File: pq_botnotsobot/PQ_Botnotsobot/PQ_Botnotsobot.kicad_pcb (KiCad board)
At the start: 2 copper layers, 64 x 58 mm, 0 parts

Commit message: Functional revision and finishing touches part I
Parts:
- added Annotation1: Silkscreen_Annotation, symbols-nsl:NSL_long, B.Cu at (101.7, 89.6)
- added Annotation2: Silkscreen_Annotation, symbols-nsl:NSL_long, B.Cu at (101.8, 35.2)
- added Annotation3: Silkscreen_Annotation, symbols-nsl:NSL_long, F.Cu at (101.8, 35.1)
- added Annotation4: Silkscreen_Annotation, symbols-nsl:NSL_long, F.Cu at (103.2, 89.5)
- added Annotation5: Silkscreen_Annotation, symbols-nsl:GRSS, F.Cu at (131.5, 54.1)
- added Annotation6: Silkscreen_Annotation, symbols-nsl:IEEE_logo, F.Cu at (131.4, 66.7)
- added Annotation7: Silkscreen_Annotation, symbols-nsl:Bridgemaker, F.Cu at (122.1, 62.1)
- added H1: MountingHole_Pad, MountingHole:MountingHole_2.2mm_M2_Pad, F.Cu at (95.5, 83.3)
- added H2: MountingHole_Pad, MountingHole:MountingHole_2.2mm_M2_Pad, F.Cu at (109.5, 83.3)
- added H3: MountingHole_Pad, MountingHole:MountingHole_2.2mm_M2_Pad, F.Cu at (123.5, 72.3)
- added H4: MountingHole_Pad, MountingHole:MountingHole_2.2mm_M2_Pad, F.Cu at (123.5, 52.3)
- added H5: MountingHole_Pad, MountingHole:MountingHole_2.2mm_M2_Pad, F.Cu at (109.5, 41.3)
- added H6: MountingHole_Pad, MountingHole:MountingHole_2.2mm_M2_Pad, F.Cu at (95.5, 41.3)
- added J1: D2FLA, miscelaneous-nsl:D2FLA, F.Cu at (132.6, 78.3)
- added J2: D2FLA1, miscelaneous-nsl:D2FLA1, F.Cu at (132.6, 46.3)
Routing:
- net (no net): vias 190 -> 0
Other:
- board text added: "DEPLOYER SLIDER PLATE"
- board text removed: "SLIDING BACKPLATE"

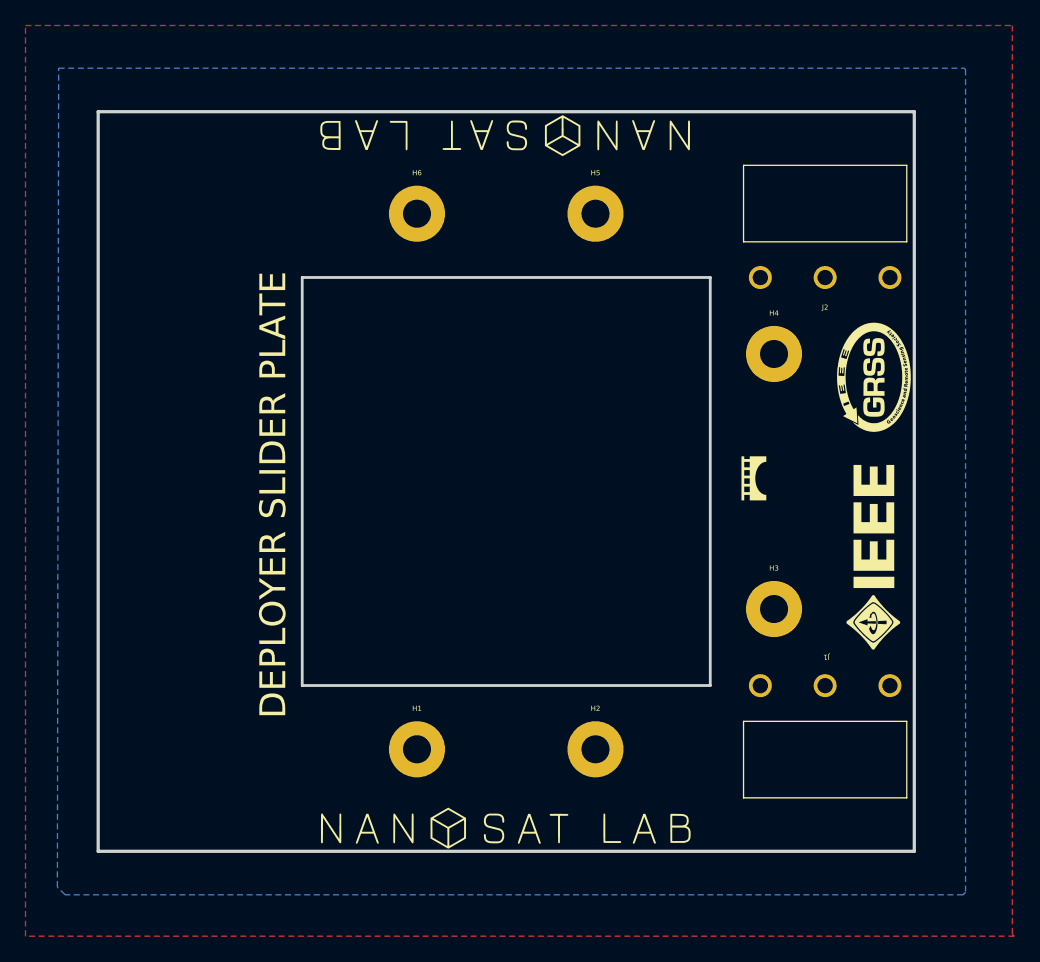
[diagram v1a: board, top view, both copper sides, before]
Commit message: Full Kicad7 transition, library improvement and adaptation, correct footprints and 3D models added
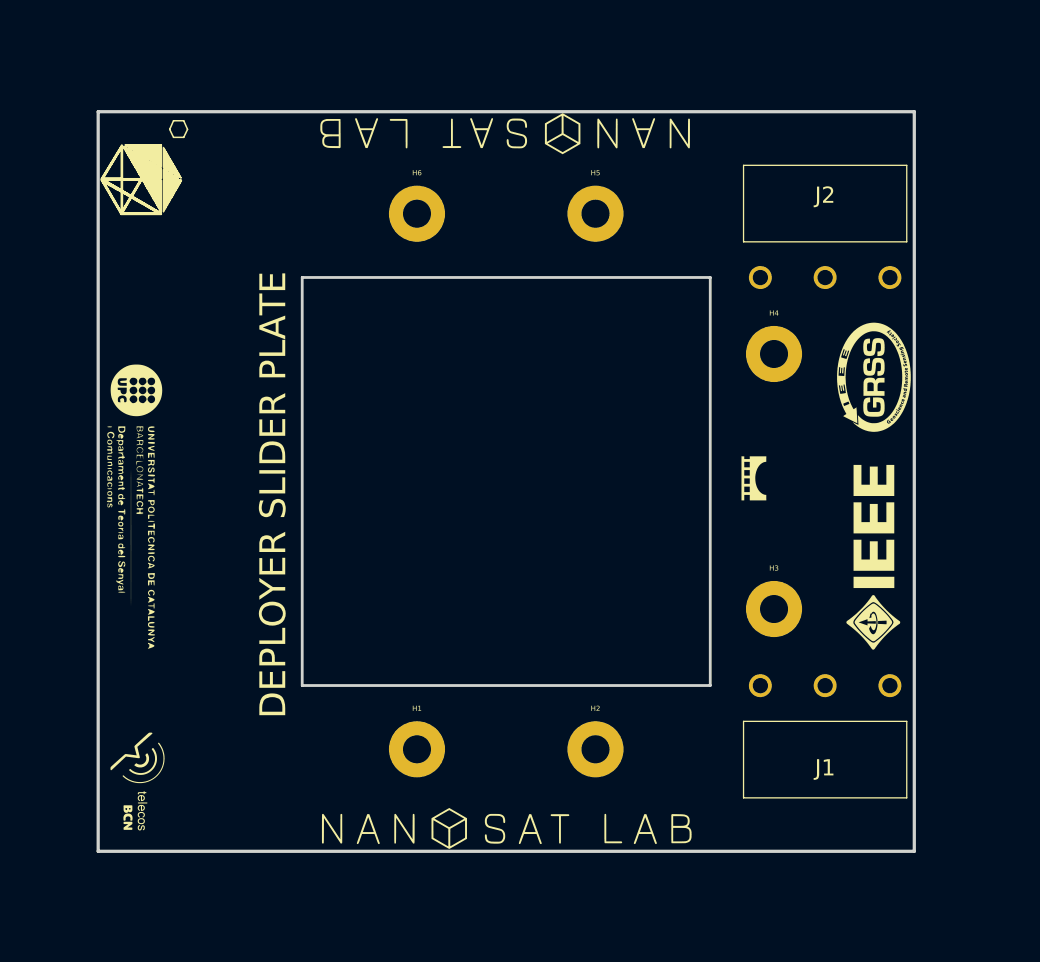
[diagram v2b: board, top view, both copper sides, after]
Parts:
- added Annotation10: Silkscreen_Annotation, -nsl_symbols:NSL, F.Cu at (80.1, 42.7)
- added Annotation8: Silkscreen_Annotation, -nsl_symbols:UPC_positiu, F.Cu at (73.1, 64.0)
- added Annotation9: Silkscreen_Annotation, -nsl_symbols:Telecos, F.Cu at (73.6, 86.1)
- Annotation1, Annotation2, Annotation3, Annotation4: footprint symbols-nsl:NSL_long -> -nsl_symbols:NSL_long
- Annotation5: footprint symbols-nsl:GRSS -> -nsl_symbols:GRSS
- Annotation6: footprint symbols-nsl:IEEE_logo -> -nsl_symbols:IEEE_logo
- Annotation7: footprint symbols-nsl:Bridgemaker -> -nsl_symbols:Bridgemaker
- J1: footprint miscelaneous-nsl:D2FLA -> -nsl_miscellaneous:D2FLA
- J2: footprint miscelaneous-nsl:D2FLA1 -> -nsl_miscellaneous:D2FLA1
- moved Annotation1 0.23 mm to (101.9, 89.6)
- moved Annotation3 0.15 mm to (101.8, 34.9)
- moved Annotation2 0.10 mm to (101.8, 35.1)
- moved Annotation4 0.08 mm to (103.2, 89.6)
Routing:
- removed copper zone on B.Cu, net (none)
- removed copper zone on F.Cu, net (none)

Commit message: fabrication ready
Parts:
- removed Annotation10: Silkscreen_Annotation, -nsl_symbols:NSL
- Annotation5: footprint -nsl_symbols:GRSS -> symbols-nsl:GRSS
- moved Annotation8 8.51 mm to (73.1, 55.4)
- moved Annotation9 8.51 mm to (73.5, 77.6)

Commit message: step and files created for all subsystems
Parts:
- removed Annotation7: Silkscreen_Annotation, -nsl_symbols:Bridgemaker
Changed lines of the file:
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@@
     (grid_origin 70.4596 91.3892)
     (pcbplotparams
-      (layerselection 0x00010fc_ffffffff)
+      (layerselection 0x0001030_7ffffffe)
       (plot_on_all_layers_selection 0x0000000_00000000)
       (disableapertmacros false)
@@
       (hpglpendiameter 15.000000)
       (dxfpolygonmode true)
-      (dxfimperialunits true)
+      (dxfimperialunits false)
       (dxfusepcbnewfont true)
       (psnegative false)
@@
       (sketchpadsonfab false)
       (subtractmaskfromsilk false)
-      (outputformat 1)
+      (outputformat 3)
       (mirror false)
-      (drillshape 1)
+      (drillshape 0)
       (scaleselection 1)
-      (outputdirectory "")
+      (outputdirectory "../../assembly/slider/")
     )
   )
@@
       )
     )
-  )
-  (footprint "-nsl_symbols:Bridgemaker" (layer "F.Cu")
-    (at 122.062381 62.072669 90)
-    (property "Sheetfile" "PQ_Botnotsobot.kicad_sch")
-    (property "Sheetname" "")
-    (attr smd)
-    (fp_text reference "Annotation7" (at 0 -0.5 90 unlocked) (layer "F.SilkS") hide
-        (effects (font (size 1 1) (thickness 0.15)))
-    )
-    (fp_text value "Silkscreen_Annotation" (at 0 1.905 90 unlocked) (layer "F.Fab")
-        (effects (font (size 1 1) (thickness 0.15)))
-    )
-    (fp_text user "${REFERENCE}" (at 0 3.175 90 unlocked) (layer "F.Fab")
-        (effects (font (size 1 1) (thickness 0.15)))
-    )
-    (fp_poly
-      (pts
-        (xy 1.77448 -0.846525)
-        (xy 1.559286 -0.846525)
-        (xy 1.559286 -0.416136)
-        (xy 1.77448 -0.416136)
-        (xy 1.77448 0.882086)
-        (xy 1.55858 0.881381)
-        (xy 1.342327 0.880322)
-        (xy 1.339858 0.839753)
-        (xy 1.338186 0.818605)
-        (xy 1.335689 0.797501)
-        (xy 1.328251 0.75547)
-        (xy 1.317606 0.71375)
-        (xy 1.303819 0.672431)
-        (xy 1.286952 0.631602)
-        (xy 1.267069 0.591353)
-        (xy 1.244231 0.551771)
-        (xy 1.218502 0.512948)
-        (xy 1.189946 0.474973)
-        (xy 1.158625 0.437934)
-        (xy 1.124603 0.401922)
-        (xy 1.087941 0.367025)
-        (xy 1.048705 0.333334)
-        (xy 1.006955 0.300936)
-        (xy 0.962757 0.269923)
-        (xy 0.916172 0.240383)
-        (xy 0.882037 0.220457)
-        (xy 0.847108 0.201427)
-        (xy 0.811392 0.183295)
-        (xy 0.774895 0.166063)
-        (xy 0.737625 0.149735)
-        (xy 0.69959 0.134312)
-        (xy 0.660795 0.119798)
-        (xy 0.621249 0.106196)
-        (xy 0.58096 0.093506)
-        (xy 0.539933 0.081733)
-        (xy 0.498176 0.070879)
-        (xy 0.455698 0.060946)
-        (xy 0.412503 0.051937)
-        (xy 0.368601 0.043855)
-        (xy 0.323999 0.036702)
-        (xy 0.278702 0.030481)
-        (xy 0.219963 0.024359)
-        (xy 0.156851 0.020267)
-        (xy 0.090745 0.018184)
-        (xy 0.023027 0.018089)
-        (xy -0.044923 0.019963)
-        (xy -0.111723 0.023783)
-        (xy -0.175994 0.029531)
-        (xy -0.236353 0.037183)
-        (xy -0.326021 0.052787)
-        (xy -0.413087 0.072497)
-        (xy -0.497298 0.096147)
-        (xy -0.578399 0.12357)
-        (xy -0.656137 0.154597)
-        (xy -0.693665 0.171411)
-        (xy -0.730258 0.189063)
-        (xy -0.765883 0.207532)
-        (xy -0.800508 0.226798)
-        (xy -0.834103 0.246839)
-        (xy -0.866635 0.267636)
-        (xy -0.898072 0.289166)
-        (xy -0.928383 0.311409)
-        (xy -0.957536 0.334343)
-        (xy -0.985499 0.357949)
-        (xy -1.012242 0.382205)
-        (xy -1.03773 0.407091)
-        (xy -1.061935 0.432584)
-        (xy -1.084822 0.458665)
-        (xy -1.106362 0.485312)
-        (xy -1.126521 0.512504)
-        (xy -1.145269 0.540221)
-        (xy -1.162573 0.568442)
-        (xy -1.178403 0.597145)
-        (xy -1.192725 0.62631)
-        (xy -1.205509 0.655916)
-        (xy -1.216723 0.685942)
-        (xy -1.223324 0.705863)
-        (xy -1.229119 0.725453)
-        (xy -1.234129 0.744778)
-        (xy -1.238374 0.763906)
-        (xy -1.241875 0.7829)
-        (xy -1.244653 0.801829)
-        (xy -1.246727 0.820758)
-        (xy -1.24812 0.839753)
-        (xy -1.250589 0.880322)
-        (xy -1.466489 0.881381)
-        (xy -1.682742 0.882086)
-        (xy -1.682742 -0.416136)
-        (xy -1.252353 -0.416136)
-        (xy -1.033631 -0.416136)
-        (xy -0.603242 -0.416136)
-        (xy -0.38452 -0.416136)
-        (xy 0.045869 -0.416136)
-        (xy 0.261063 -0.416136)
-        (xy 0.69498 -0.416136)
-        (xy 0.910175 -0.416136)
-        (xy 1.340563 -0.416136)
-        (xy 1.340563 -0.846525)
-        (xy 0.910175 -0.846525)
-        (xy 0.910175 -0.416136)
-        (xy 0.69498 -0.416136)
-        (xy 0.69498 -0.846525)
-        (xy 0.261063 -0.846525)
-        (xy 0.261063 -0.416136)
-        (xy 0.045869 -0.416136)
-        (xy 0.045869 -0.846525)
-        (xy -0.38452 -0.846525)
-        (xy -0.38452 -0.416136)
-        (xy -0.603242 -0.416136)
-        (xy -0.603242 -0.846525)
-        (xy -1.033631 -0.846525)
-        (xy -1.033631 -0.416136)
-        (xy -1.252353 -0.416136)
-        (xy -1.252353 -0.846525)
-        (xy -1.682742 -0.846525)
-        (xy -1.682742 -1.065247)
-        (xy 1.77448 -1.065247)
-      )
-      (stroke (width 0) (type solid)) (fill solid) (layer "F.SilkS"))
-    (group "" (id 0cca56bb-c39a-46bc-b23d-c82935ec7dbb)
-      (members
-        d1500102-69a6-403f-b114-785dc9068fa0
-      )
-    )
